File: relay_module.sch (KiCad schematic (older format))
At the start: 10 parts, among them J1 Screw_Terminal_1x02, J2 Screw_Terminal_1x02, J3 Screw_Terminal_1x03, Q1 Q_NMOS_DGS

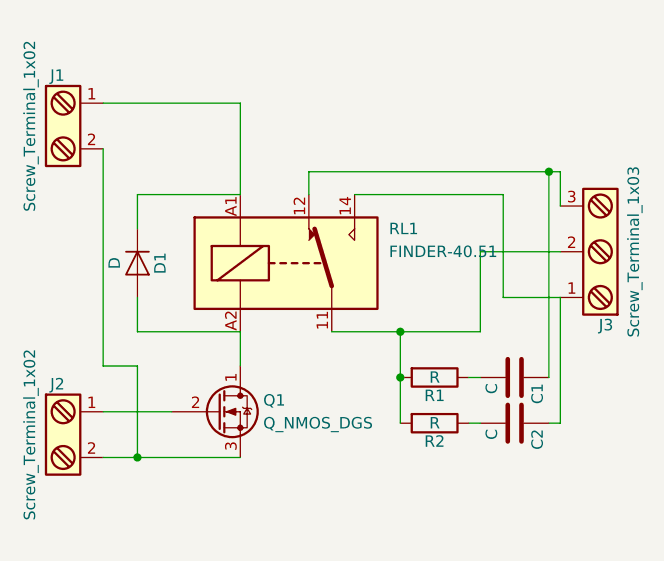
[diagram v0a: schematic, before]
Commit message: add pull-down resistor for transitor
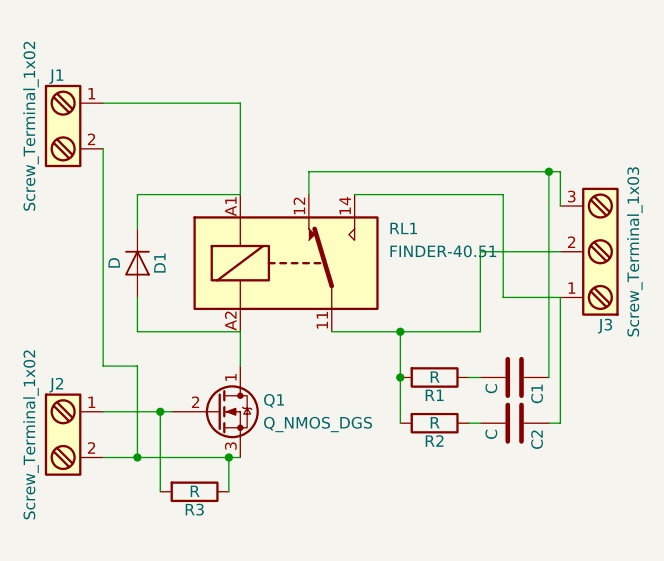
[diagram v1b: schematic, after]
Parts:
- added R3: R, Resistors_THT:R_Axial_DIN0207_L6.3mm_D2.5mm_P7.62mm_Horizontal, symbol R
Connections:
- net at J1.2, J2.2, Q1.3 (S): now also R3.1
- net at J2.1, Q1.2 (G): now also R3.2
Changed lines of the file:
@@
 	4550 3850 4550 4000
 Wire Wire Line
-	4550 4400 3950 4400
+	3950 4400 4550 4400
 Wire Wire Line
 	3950 4200 4250 4200
@@
 Wire Wire Line
 	4550 2850 4550 3250
+$Comp
+L R R3
+U 1 1 5A0727D4
+P 4350 4550
+F 0 "R3" V 4430 4550 50  0000 C CNN
+F 1 "R" V 4350 4550 50  0000 C CNN
+F 2 "Resistors_THT:R_Axial_DIN0207_L6.3mm_D2.5mm_P7.62mm_Horizontal" V 4280 4550 50  0001 C CNN
+F 3 "" H 4350 4550 50  0001 C CNN
+	1    4350 4550
+	0    1    1    0
+$EndComp
+Wire Wire Line
+	4200 4200 4200 4550
+Connection ~ 4200 4200
+Wire Wire Line
+	4500 4550 4500 4400
+Connection ~ 4500 4400
 $EndSCHEMATC
